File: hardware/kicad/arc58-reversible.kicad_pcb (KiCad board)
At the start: 2 copper layers, 169.3 x 152.2 mm, 91 parts, among them J1 MJ-4PP-9_Reversible, J2 SSD1306 OLED 128x32, SW1 SW_PUSH_LED, SW10 SW_PUSH_LED, SW11 SW_PUSH_LED, SW12 SW_PUSH_LED, SW13 SW_PUSH_LED, SW14 SW_PUSH_LED, SW15 SW_PUSH_LED, SW16 SW_PUSH_LED, SW17 SW_PUSH_LED, SW18 SW_PUSH_LED, SW19 SW_PUSH_LED, SW2 SW_PUSH_LED, SW20 SW_PUSH_LED, SW21 SW_PUSH_LED, SW22 SW_PUSH_LED, SW23 SW_PUSH_LED, SW24 SW_PUSH_LED, SW25 Rotary_Encoder_Switch, SW26 SW_PUSH_LED, SW27 SW_PUSH_LED, SW28 SW_PUSH_LED, SW29 SW_PUSH_LED, SW3 SW_PUSH_LED, SW4 SW_PUSH_LED, SW5 SW_PUSH_LED, SW6 SW_PUSH_LED, SW7 SW_PUSH_LED, SW8 SW_PUSH_LED, SW9 SW_PUSH_LED, U1 KEEBD Helios RP2040, U2 74AHCT1G125

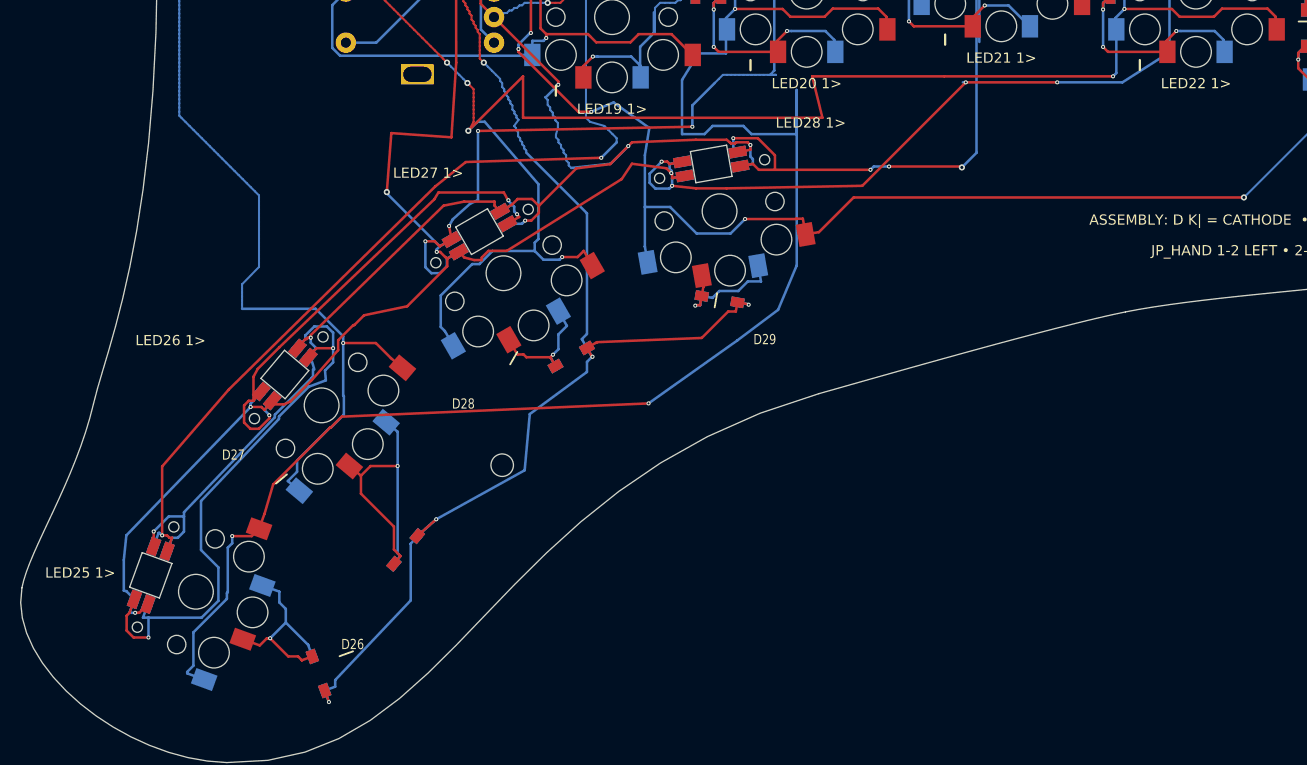
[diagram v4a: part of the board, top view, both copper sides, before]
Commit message: Tighten thumb key spacing
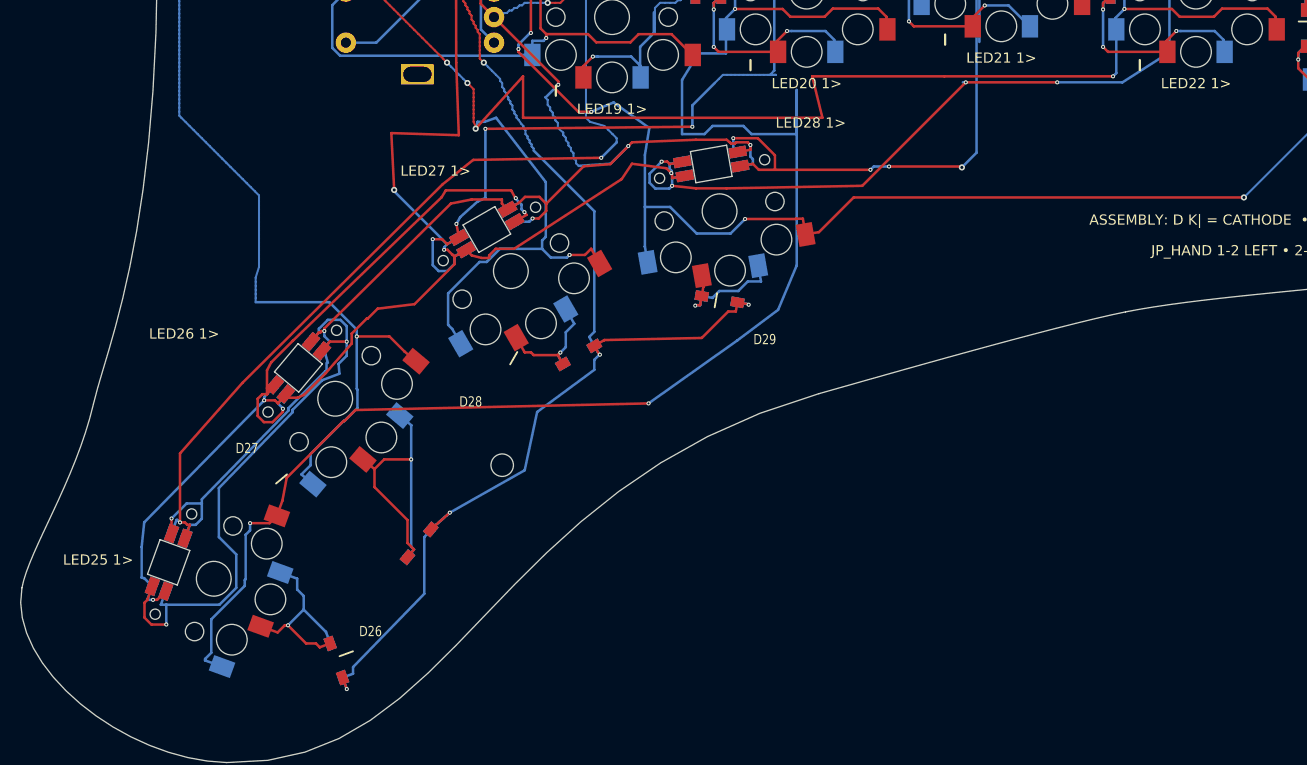
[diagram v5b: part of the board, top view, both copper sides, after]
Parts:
- moved D26 2.16 mm to (93.6, 170.1)
- moved SW26 2.16 mm to (81.6, 162.1)
- moved D27 1.48 mm to (101.7, 158.6)
- moved SW27 1.48 mm to (93.5, 144.5)
- moved D28 0.75 mm to (117.3, 140.2)
- moved SW28 0.75 mm to (110.6, 132.0)
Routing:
- net GND: track 1181.6 -> 1178.7 mm
- net ROW4: track 175.4 -> 172.5 mm
- net Net-(SW19-Pad2): track 96.2 -> 94.0 mm
- net COL4: track 321.0 -> 318.9 mm
- net VBUS: track 1272.6 -> 1270.8 mm
- net COL3: track 329.7 -> 328.4 mm
- net Net-(SW27-Pad2): track 49.3 -> 48.6 mm
- net Net-(SW26-Pad2): track 57.5 -> 56.8 mm
- net Net-(SW20-Pad4): track 91.5 -> 90.8 mm

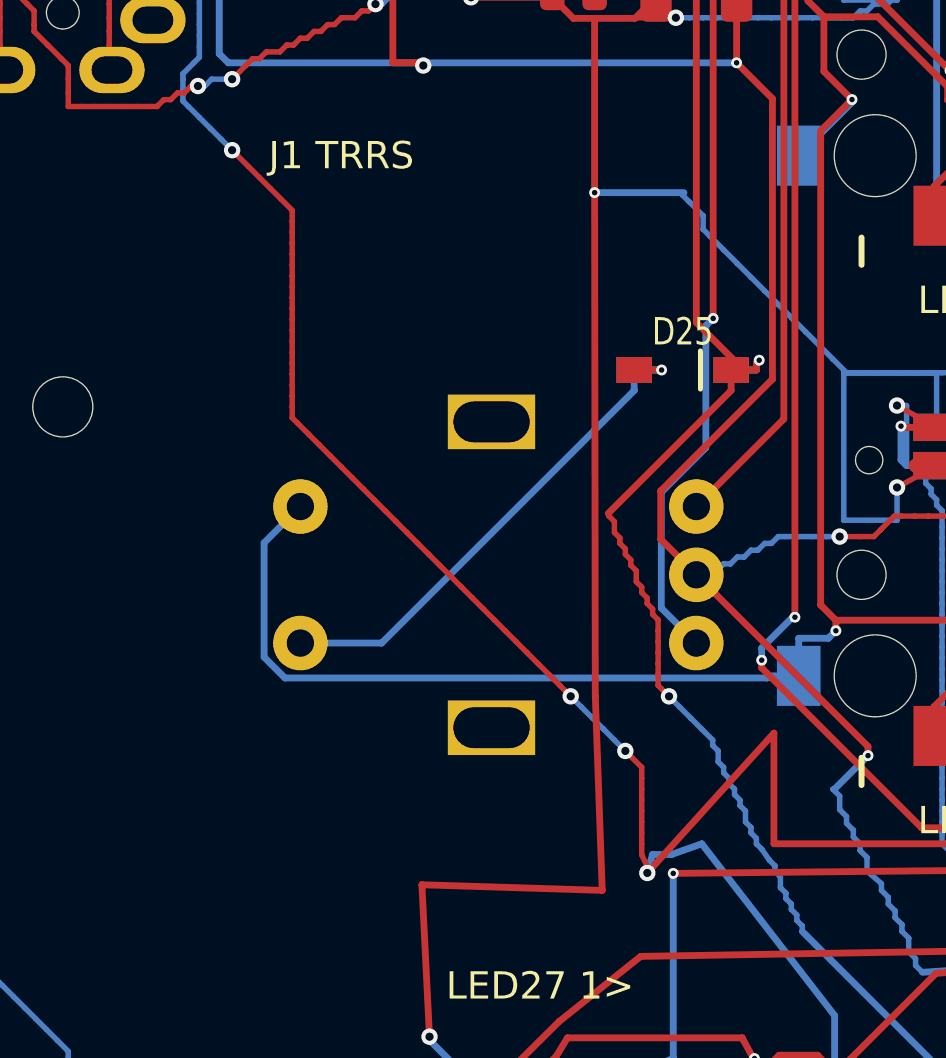
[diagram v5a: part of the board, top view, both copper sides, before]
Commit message: Move encoders inward for knob clearance
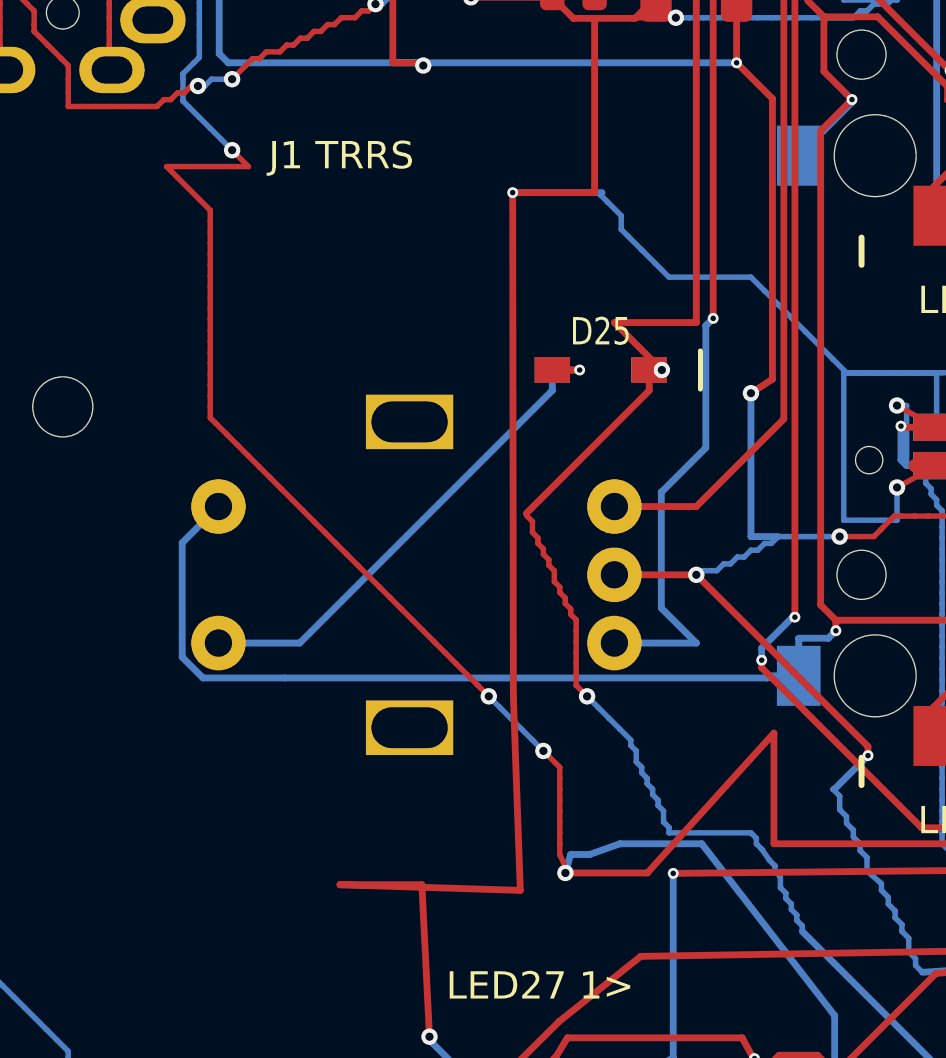
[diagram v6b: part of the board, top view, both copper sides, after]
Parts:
- moved D25 3.00 mm to (105.5, 99.7)
- moved SW25 3.00 mm to (98.5, 107.2)
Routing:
- net VBUS: track 1270.8 -> 1279.8 mm
- net COL2: track 348.8 -> 357.8 mm
- net ROW4: track 172.5 -> 176.8 mm
- net ENC_B: track 69.8 -> 72.8 mm
- net ENC_A: track 86.7 -> 89.7 mm
- net COL5: track 196.6 -> 199.6 mm
- net GND: track 1178.7 -> 1179.4 mm, vias 77 -> 79

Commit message: Center encoder clearance
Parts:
- moved H4 16.5 mm to (81.8, 117.0)
- moved D25 4.37 mm to (101.1, 99.7)
- moved SW25 4.37 mm to (94.1, 107.2)
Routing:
- net COL2: track 357.8 -> 370.9 mm
- net ENC_A: track 89.7 -> 102.8 mm
- net VBUS: track 1279.8 -> 1292.9 mm
- net COL3: track 328.4 -> 337.2 mm
- net ROW4: track 176.8 -> 185.5 mm
- net Net-(SW19-Pad2): track 94.0 -> 102.7 mm
- net GND: track 1179.4 -> 1183.8 mm
- net ENC_B: track 72.8 -> 77.2 mm
- net COL5: track 199.6 -> 204.0 mm

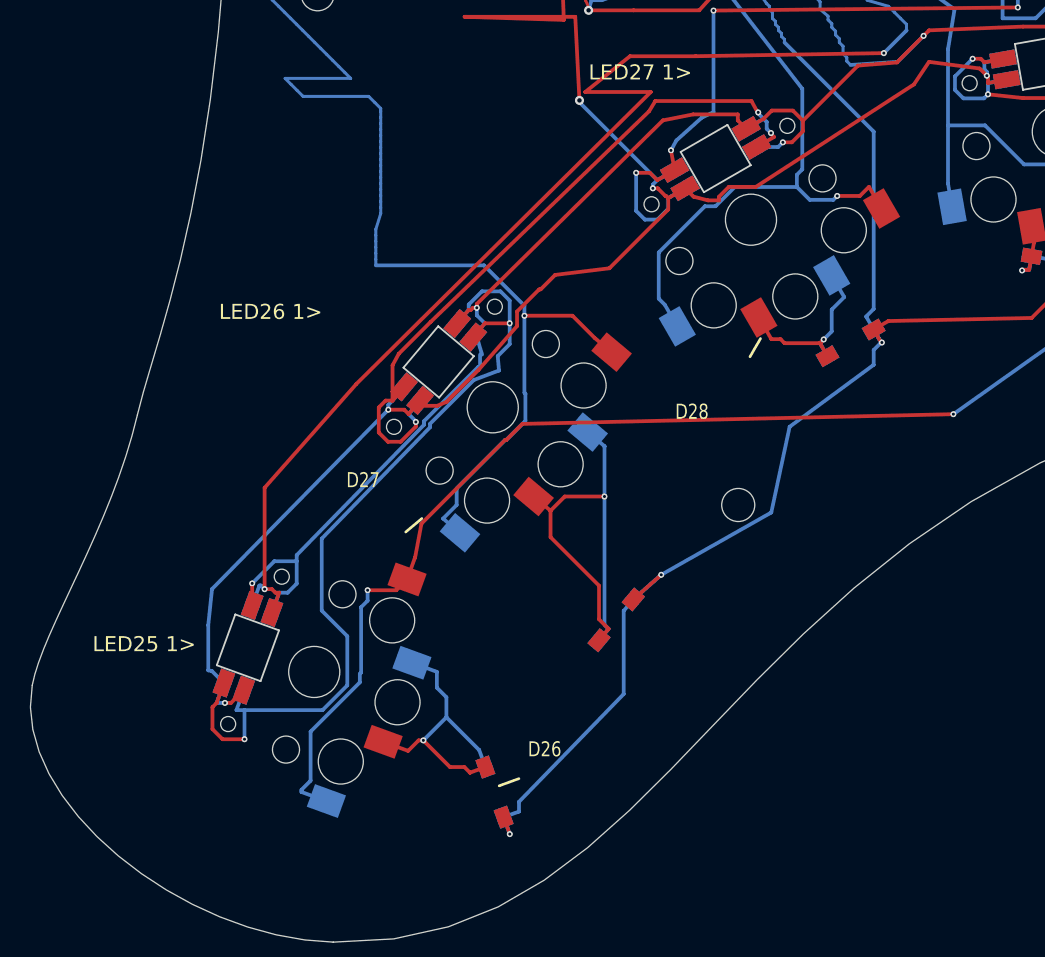
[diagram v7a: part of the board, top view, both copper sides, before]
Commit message: Refine T3 and T4 thumb sweep
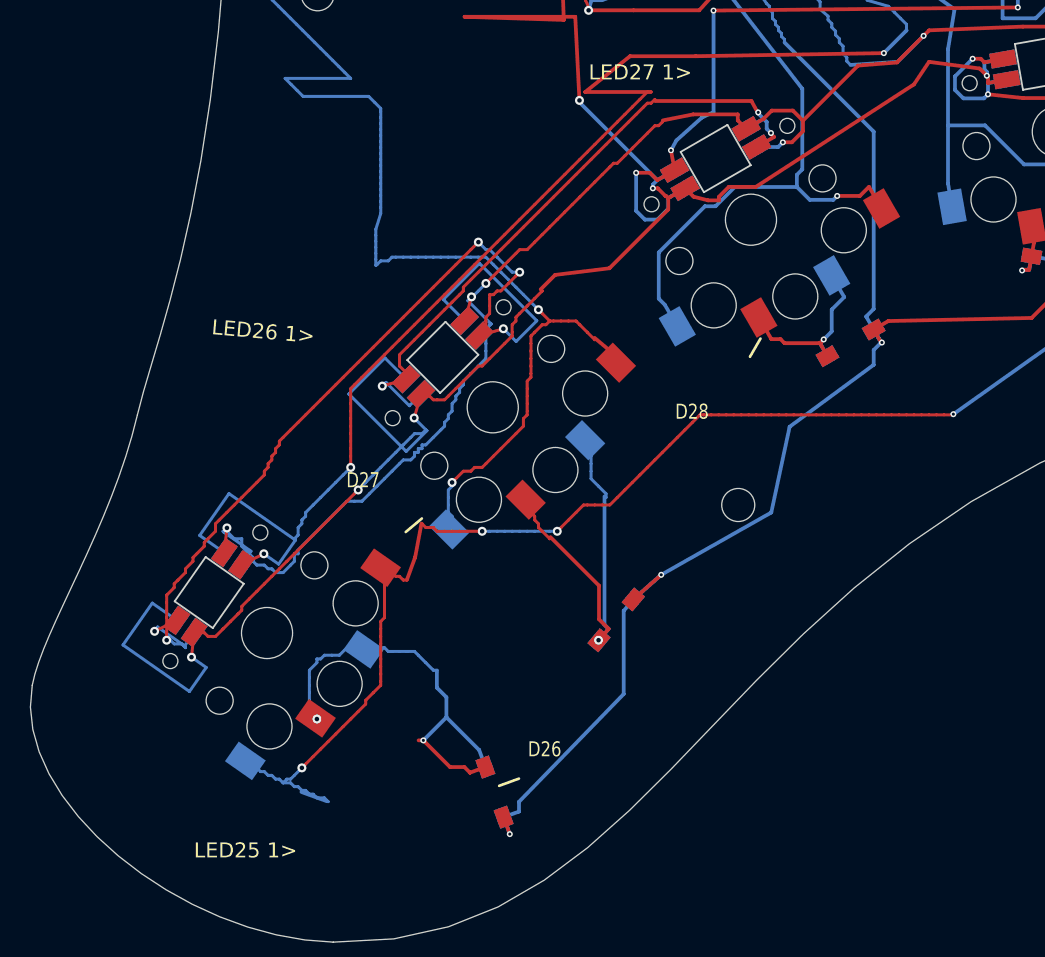
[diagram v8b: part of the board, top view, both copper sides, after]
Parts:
- moved SW26 4.07 mm to (78.4, 159.5), turned to -125 degrees
- turned SW27 to -135 degrees
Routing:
- net VBUS: track 1292.9 -> 1313.9 mm, vias 71 -> 72
- net Net-(SW26-Pad2): track 56.8 -> 66.9 mm, vias 2 -> 5
- net Net-(D26-Pad2): track 19.7 -> 29.0 mm, vias 1 -> 2
- net COL4: track 318.9 -> 327.6 mm, vias 9 -> 11
- net Net-(SW19-Pad2): track 102.7 -> 110.3 mm, vias 4 -> 5
- net GND: track 1183.8 -> 1190.3 mm, vias 79 -> 80
- net Net-(SW27-Pad2): track 48.6 -> 43.5 mm
- net Net-(D27-Pad2): track 30.7 -> 26.7 mm
- net COL3: track 337.2 -> 339.5 mm, vias 15 -> 16
